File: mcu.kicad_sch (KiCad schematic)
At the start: 0 parts

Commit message: feat: microcontroller setup with decoupling caps
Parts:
- added BZ1: Buzzer, Eagle_Main:Buzzer_TDK_SD1614TT_D16mm_H14mm_P5mm, symbol Device:Buzzer
- added C16, C17, C18, C19, C20, C21, C22, C23, C27, C6, C7, C8, C9: 100n, Capacitor_SMD:C_0603_1608Metric, symbol Device:C
- added C24: 4.7u, Capacitor_SMD:C_0805_2012Metric, symbol Device:C
- added C25, C26: 2.2u, Capacitor_SMD:C_0805_2012Metric, symbol Device:C
- added C28, C29: 1u, Capacitor_SMD:C_0805_2012Metric, symbol Device:C
- added C4, C5: C, Capacitor_SMD:C_0603_1608Metric, symbol Device:C
- added D4: 1N4148W, Diode_SMD:D_SOD-323, symbol Diode:1N4148W
- added D5, D6: LED_Small, LED_SMD:LED_0603_1608Metric, symbol Device:LED_Small
- added D7: TVS, Diode_SMD:D_SOD-523, symbol Device:D_Zener
- added IC2: STM32H723ZGT6, Package_QFP:LQFP-144_20x20mm_P0.5mm, symbol STM32H7:STM32H723ZGT6
- added J1: Conn_ST_STDC14, eagle_connectors:SAMTEC_FTSH-107-01-L-DV-K-TR, symbol Connector:Conn_ST_STDC14
- added JP1: BOOT0, Jumper:SolderJumper-3_P1.3mm_Open_RoundedPad1.0x1.5mm, symbol Jumper:SolderJumper_3_Open
- added Q1: 2N7002NXAKR, Package_TO_SOT_SMD:SOT-23, symbol Transistor_FET:2N7002
- added R10, R11: 1k, Resistor_SMD:R_0603_1608Metric, symbol Device:R
- added R12, R3: R, Resistor_SMD:R_0603_1608Metric, symbol Device:R
- added R4: 22R, Resistor_SMD:R_0603_1608Metric, symbol Device:R
- added R5: 100K, Resistor_SMD:R_0603_1608Metric, symbol Device:R
- added R6, R7: 100k, Resistor_SMD:R_0603_1608Metric, symbol Device:R
- added SW1: RESET, Button_Switch_SMD:SW_SPST_FSMSM, symbol Switch:SW_Push
- added Y1: 16MHz, Crystal:Crystal_SMD_EuroQuartz_MT-4Pin_3.2x2.5mm, symbol Device:Crystal_GND24
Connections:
- new net: BZ1.2 (+), D4.2 (A), Q1.3 (D)
- new net: Q1.1 (G), R4.2, R5.2
- new net: C4.1, R3.2, Y1.1
- new net: D5.2 (A), R10.1
- new net: JP1.2 (C), R12.1
- new net: D6.2 (A), R11.1
- new net +3V3: C16.1, C17.1, C18.1, C19.1, C20.1, C21.1, C22.1, C23.1, C24.1, C27.1, C28.1, C29.1, C7.1, C8.1, C9.1, IC2.108 (VDD_8), IC2.121 (VDD_9), IC2.131 (VDD_10), IC2.144 (VDD_11), IC2.17 (VDD_1), IC2.32 (VREF+), IC2.33 (VDDA), IC2.39 (VDD_3), IC2.52 (VDD_4), IC2.62 (VDD_5), IC2.72 (VDD_6), IC2.84 (VDD_7), J1.3 (VCC), JP1.1 (A), R6.2
- new net +5V: BZ1.1 (-), D4.1 (K)
- new net 3V3_PROBING: R6.1, R7.2
- new net BOOT0: IC2.138 (BOOT0), R12.2
- new net BUZZER: R4.1
- new net GND: C16.2, C17.2, C18.2, C19.2, C20.2, C21.2, C22.2, C23.2, C24.2, C25.2, C26.2, C27.2, C28.2, C29.2, C4.2, C5.2, C6.2, C7.2, C8.2, C9.2, D5.1 (K), D6.1 (K), D7.2 (A), IC2.107 (VSS_7), IC2.120 (VSS_8), IC2.130 (VSS_9), IC2.16 (VSS_1), IC2.31 (VSSA), IC2.38 (VSS_2), IC2.51 (VSS_3), IC2.61 (VSS_4), IC2.83 (VSS_5), J1.11 (GNDDetect), J1.5 (GND), J1.7 (GND), JP1.3 (B), Q1.2 (S), R5.1, R7.1, SW1.1, Y1.2, Y1.4
- new net LED_1: R10.2
- new net LED_2: R11.2
- new net OSC_IN: C5.1, IC2.23 (PH0-OSC_IN), Y1.3
- new net OSC_OUT: IC2.24 (PH1-OSC_OUT), R3.1
- new net RX_SWD: J1.13 (VCP_RX)
- new net SWCLK: J1.6 (JCLK/SWCLK)
- new net SWDIO: J1.4 (JTMS/SWDIO)
- new net TX_SWD: J1.14 (VCP_TX)
- new net VCAP1: C25.1, IC2.71 (VCAP_1)
- new net VCAP2: C26.1, IC2.106 (VCAP_2)
- new net ~{RST}: C6.1, D7.1 (K), IC2.25 (NRST), J1.12 (~{RST}), SW1.2
- no-connect marks 0 -> 3
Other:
- note added: "3V3 probing divider"
- note added: "Analog supply"
- note added: "BOOT0"
- note added: "Bulk cap"
- note added: "Buzzer"
- note added: "Crystal"
- note added: "Debugger"
- note added: "Decoupling"
- note added: "Internal regulator capacitors"
- note added: "LEDs signals"
- note added: "PB8-BOOT0 pin configuration: LOW: normal, boot from user flash HIGH: boot from system memory, bootloader"
- note added: "RESET"
- note added: "Supply decoupling"

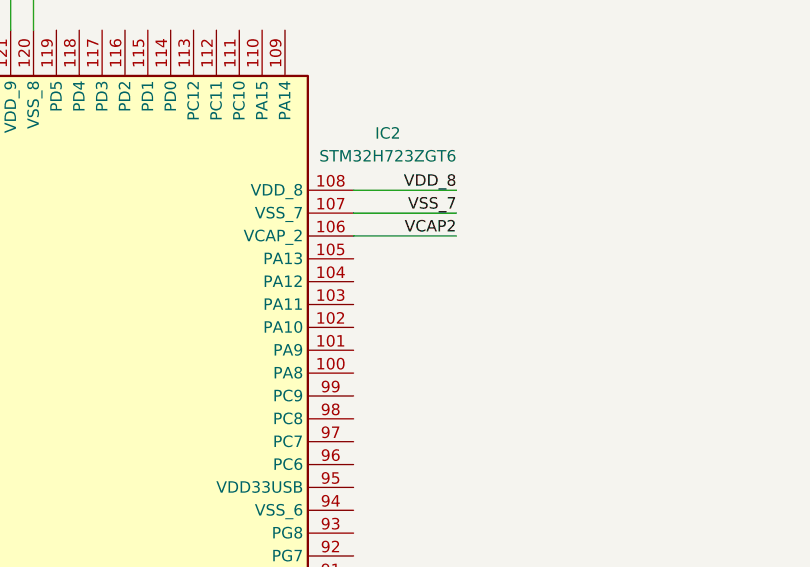
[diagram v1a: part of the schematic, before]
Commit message: feat: voltage divider on UA96 inputs from new llinear encoder
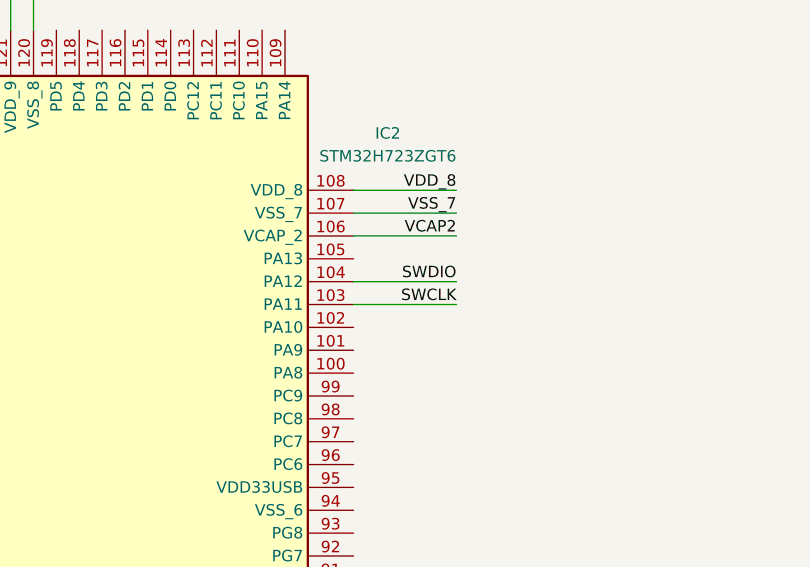
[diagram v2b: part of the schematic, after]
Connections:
- net SWCLK: now also IC2.103 (PA11)
- net SWDIO: now also IC2.104 (PA12)
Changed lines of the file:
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@@
+	(wire
+		(pts
+			(xy 261.62 110.49) (xy 273.05 110.49)
+		)
+		(stroke
+			(width 0)
+			(type default)
+		)
+	)
 	(wire
 		(pts
@@
 		(pts
 			(xy 228.6 204.47) (xy 228.6 214.63)
+		)
+		(stroke
+			(width 0)
+			(type default)
+		)
+	)
+	(wire
+		(pts
+			(xy 261.62 107.95) (xy 273.05 107.95)
 		)
 		(stroke
@@
 		)
 	)
+	(label "SWDIO"
+		(at 273.05 107.95 180)
+		(effects
+			(font
+				(size 1.27 1.27)
+			)
+			(justify right bottom)
+		)
+	)
 	(label "VREF+"
 		(at 146.05 176.53 0)
@@
 		(effects
 			(font
+				(size 1.27 1.27)
+			)
+			(justify right bottom)
+		)
+	)
+	(label "SWCLK"
+		(at 273.05 110.49 180)
+		(effects
+			(font

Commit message: fix: minors
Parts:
- removed BZ1: Buzzer, Eagle_Main:Buzzer_TDK_SD1614TT_D16mm_H14mm_P5mm, symbol Device:Buzzer
- removed D4: 1N4148W, Diode_SMD:D_SOD-323, symbol Diode:1N4148W
- removed Q1: 2N7002NXAKR, Package_TO_SOT_SMD:SOT-23, symbol Transistor_FET:2N7002
- removed R4: 22R, Resistor_SMD:R_0603_1608Metric, symbol Device:R
- removed R5: 100K, Resistor_SMD:R_0603_1608Metric, symbol Device:R
- removed R6, R7: 100k, Resistor_SMD:R_0603_1608Metric, symbol Device:R
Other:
- note removed: "3V3 probing divider"
- note removed: "Buzzer"
- moved on the sheet: D5, D6, R10, R11

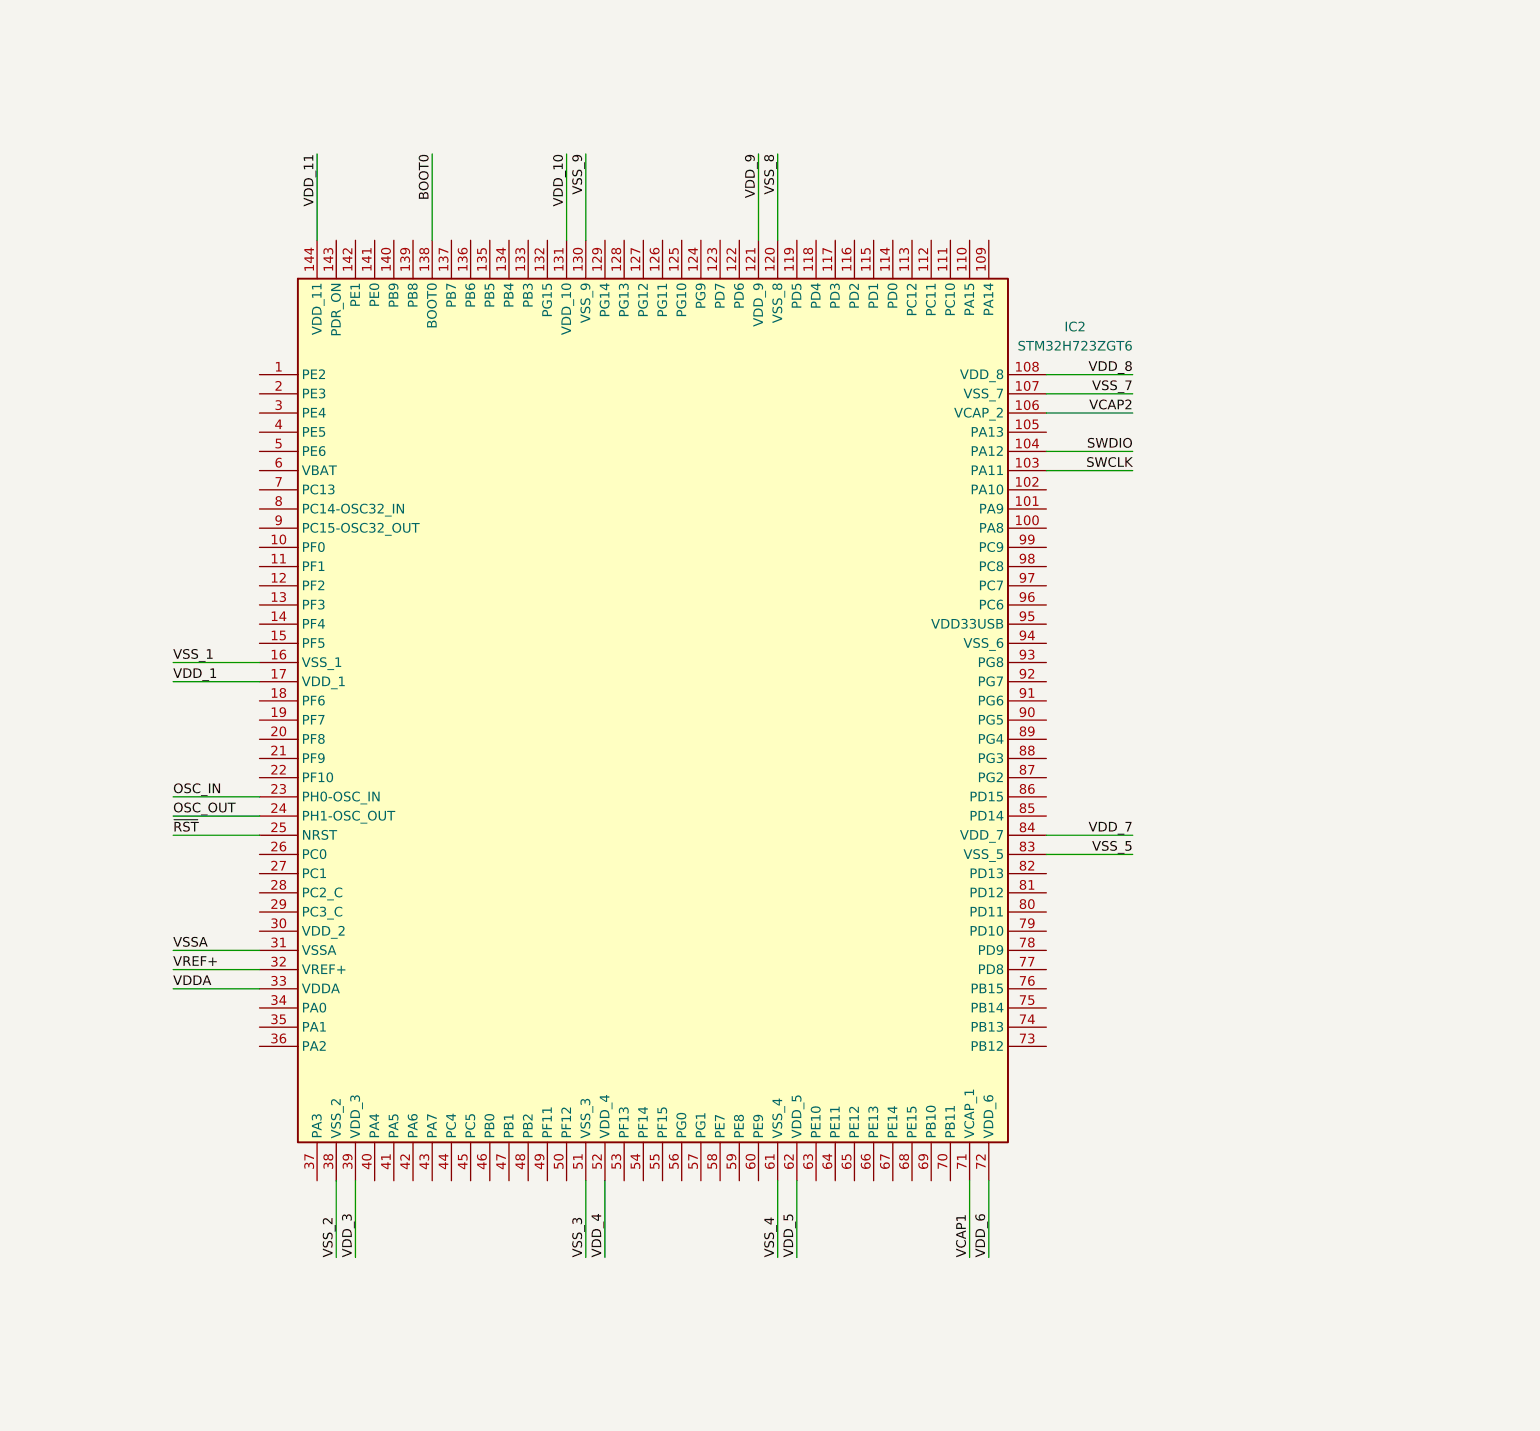
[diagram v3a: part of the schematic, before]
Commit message: feat: pwm for dcs to micro, uart
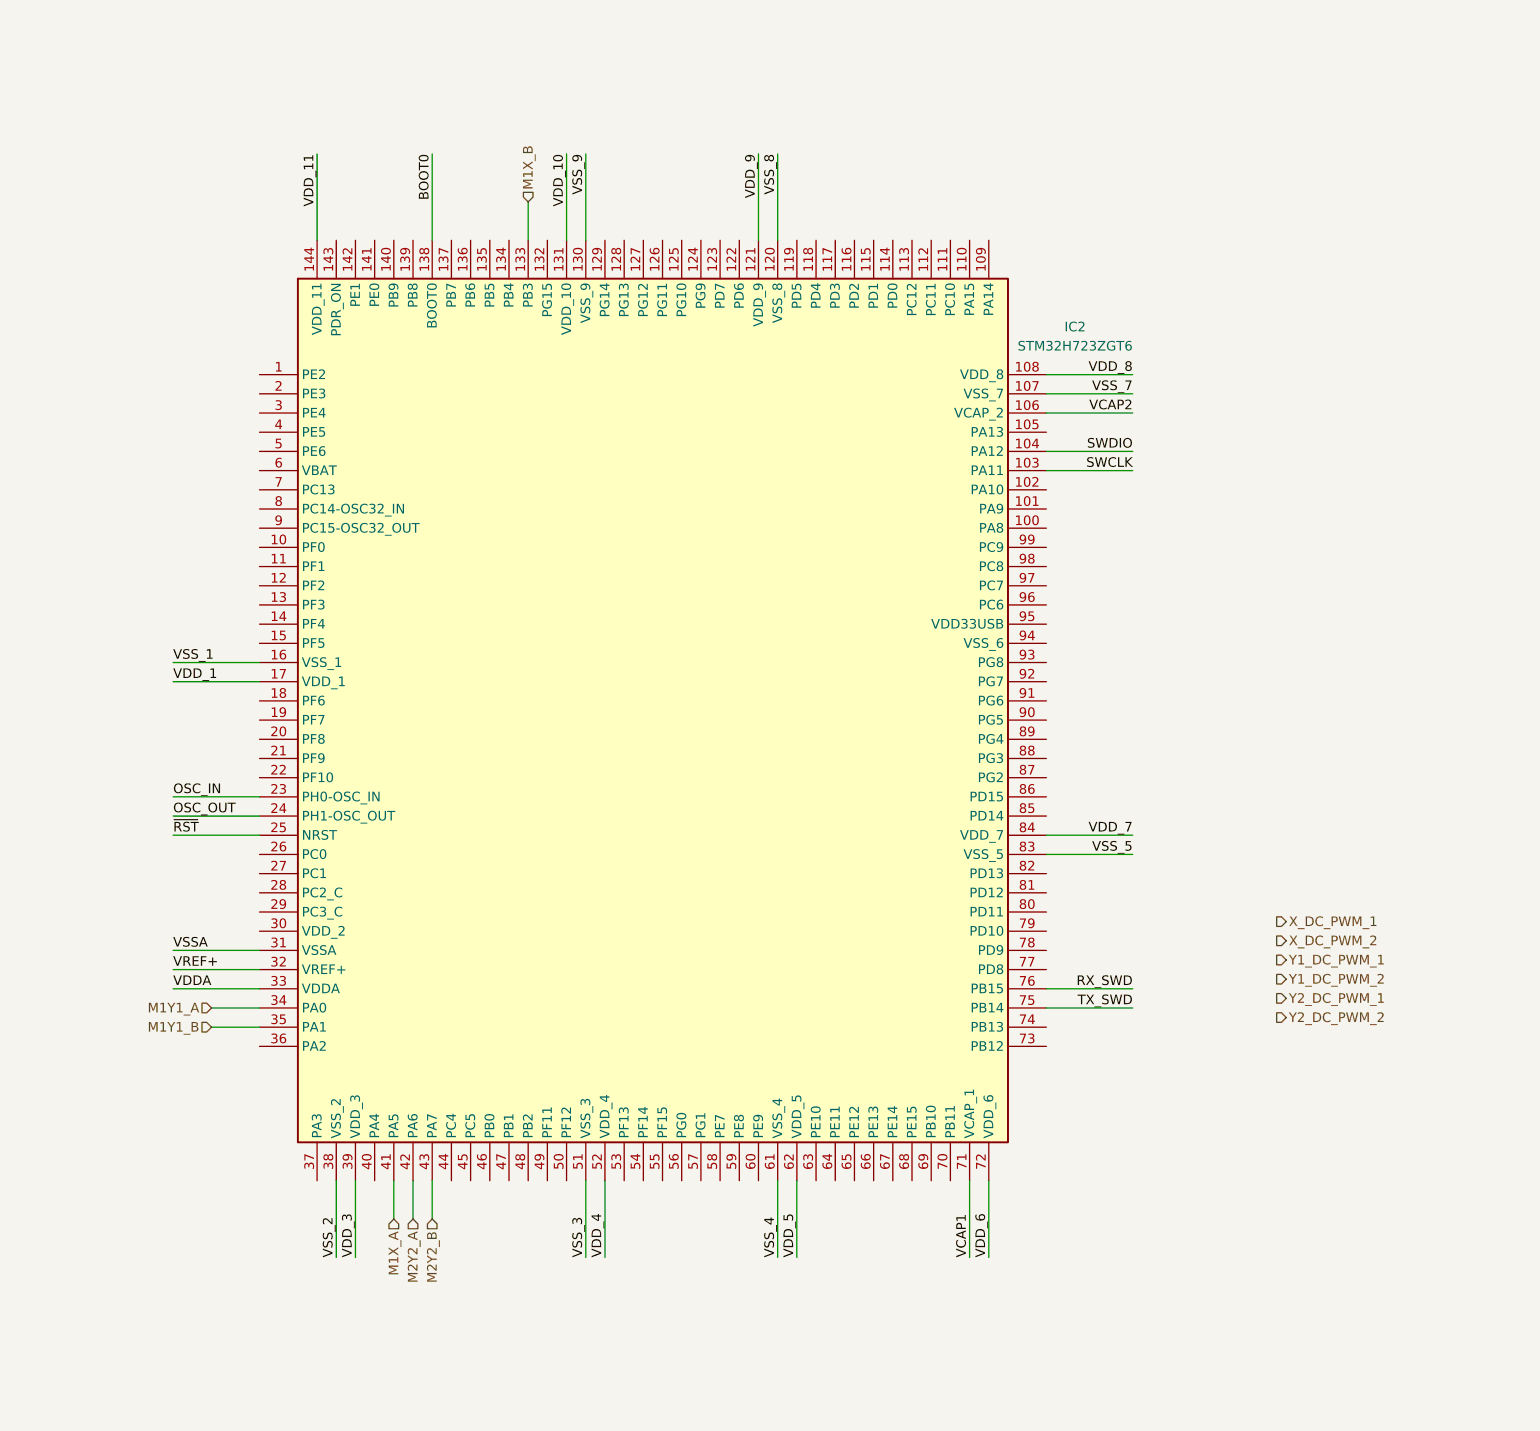
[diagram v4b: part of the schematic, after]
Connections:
- net RX_SWD: now also IC2.76 (PB15)
- net TX_SWD: now also IC2.75 (PB14)
- net M1X_B: now reaches IC2.133 (PB3)
- net M1Y1_A: now reaches IC2.34 (PA0)
- net M1Y1_B: now reaches IC2.35 (PA1)
- net M1X_A: now reaches IC2.41 (PA5)
- net M2Y2_A: now reaches IC2.42 (PA6)
- net M2Y2_B: now reaches IC2.43 (PA7)
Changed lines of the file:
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@@
+	(wire
+		(pts
+			(xy 180.34 204.47) (xy 180.34 209.55)
+		)
+		(stroke
+			(width 0)
+			(type default)
+		)
+	)
 	(wire
 		(pts
@@
 	(wire
 		(pts
+			(xy 151.13 184.15) (xy 157.48 184.15)
+		)
+		(stroke
+			(width 0)
+			(type default)
+		)
+	)
+	(wire
+		(pts
 			(xy 41.91 134.62) (xy 38.1 134.62)
 		)
@@
 	(wire
 		(pts
+			(xy 175.26 204.47) (xy 175.26 209.55)
+		)
+		(stroke
+			(width 0)
+			(type default)
+		)
+	)
+	(wire
+		(pts
 			(xy 27.94 93.98) (xy 27.94 95.25)
 		)
@@
 		)
 	)
+	(wire
+		(pts
+			(xy 261.62 181.61) (xy 273.05 181.61)
+		)
+		(stroke
+			(width 0)
+			(type default)
+		)
+	)
 	(polyline
 		(pts
@@
 	(wire
 		(pts
+			(xy 177.8 204.47) (xy 177.8 209.55)
+		)
+		(stroke
+			(width 0)
+			(type default)
+		)
+	)
+	(wire
+		(pts
 			(xy 38.1 154.94) (xy 41.91 154.94)
 		)
@@
 	(wire
 		(pts
+			(xy 151.13 181.61) (xy 157.48 181.61)
+		)
+		(stroke
+			(width 0)
+			(type default)
+		)
+	)
+	(wire
+		(pts
 			(xy 73.66 50.8) (xy 73.66 49.53)
 		)
@@
 	(wire
 		(pts
+			(xy 261.62 179.07) (xy 273.05 179.07)
+		)
+		(stroke
+			(width 0)
+			(type default)
+		)
+	)
+	(wire
+		(pts
 			(xy 67.31 199.39) (xy 67.31 198.12)
 		)
@@
 		(pts
 			(xy 180.34 68.58) (xy 180.34 80.01)
+		)
+		(stroke
+			(width 0)
+			(type default)
+		)
+	)
+	(wire
+		(pts
+			(xy 193.04 74.93) (xy 193.04 80.01)
 		)
 		(stroke
@@
 		)
 	)
+	(label "TX_SWD"
+		(at 273.05 181.61 180)
+		(effects
+			(font
+				(size 1.27 1.27)
+			)
+			(justify right bottom)
+		)
+	)
 	(label "LED_2"
 		(at 389.89 133.35 0)
@@
 		)
 	)
+	(label "RX_SWD"
+		(at 273.05 179.07 180)
+		(effects
+			(font
+				(size 1.27 1.27)
+			)
+			(justify right bottom)
+		)
+	)
 	(label "VCAP2"
 		(at 273.05 102.87 180)
@@
 		)
 	)
+	(hierarchical_label "X_DC_PWM_1"
+		(shape output)
+		(at 292.1 170.18 0)
+		(effects
+			(font
+				(size 1.27 1.27)
+			)
+			(justify left)
+		)
+	)
+	(hierarchical_label "M2Y2_A"
+		(shape input)
+		(at 177.8 209.55 270)
+		(effects
+			(font
+				(size 1.27 1.27)
+			)
+			(justify right)
+		)
+	)
+	(hierarchical_label "M1X_B"
+		(shape input)
+		(at 193.04 74.93 90)
+		(effects
+			(font
+				(size 1.27 1.27)
+			)
+			(justify left)
+		)
+	)
+	(hierarchical_label "X_DC_PWM_2"
+		(shape output)
+		(at 292.1 172.72 0)
+		(effects
+			(font
+				(size 1.27 1.27)
+			)
+			(justify left)
+		)
+	)
+	(hierarchical_label "M1X_A"
+		(shape input)
+		(at 175.26 209.55 270)
+		(effects
+			(font
+				(size 1.27 1.27)
+			)
+			(justify right)
+		)
+	)
+	(hierarchical_label "Y1_DC_PWM_2"
+		(shape output)
+		(at 292.1 177.8 0)
+		(effects
+			(font
+				(size 1.27 1.27)
+			)
+			(justify left)
+		)
+	)
+	(hierarchical_label "Y2_DC_PWM_1"
+		(shape output)
+		(at 292.1 180.34 0)
+		(effects
+			(font
+				(size 1.27 1.27)
+			)
+			(justify left)
+		)
+	)
+	(hierarchical_label "M1Y1_B"
+		(shape input)
+		(at 151.13 184.15 180)
+		(effects
+			(font
+				(size 1.27 1.27)
+			)
+			(justify right)
+		)
+	)
+	(hierarchical_label "Y2_DC_PWM_2"
+		(shape output)
+		(at 292.1 182.88 0)
+		(effects
+			(font
+				(size 1.27 1.27)
+			)
+			(justify left)
+		)
+	)
+	(hierarchical_label "M1Y1_A"
+		(shape input)
+		(at 151.13 181.61 180)
+		(effects
+			(font
+				(size 1.27 1.27)
+			)
+			(justify right)
+		)
+	)
+	(hierarchical_label "Y1_DC_PWM_1"
+		(shape output)
+		(at 292.1 175.26 0)
+		(effects
+			(font
+				(size 1.27 1.27)
+			)
+			(justify left)
+		)
+	)
+	(hierarchical_label "M2Y2_B"
+		(shape input)
+		(at 180.34 209.55 270)
+		(effects
+			(font
+				(size 1.27 1.27)
+			)
+			(justify right)
+		)
+	)

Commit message: feat: setup spi
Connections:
- net SWCLK: now also IC2.109 (PA14); no longer IC2.103 (PA11)
- net SWDIO: now also IC2.105 (PA13); no longer IC2.104 (PA12)
- net SPI1_MOSI: now reaches IC2.123 (PD7)
- net SPI1_MISO: now reaches IC2.124 (PG9)
- net SPI1_SCK: now reaches IC2.126 (PG11)
- net SPI2_MOSI: now reaches IC2.27 (PC1)
- net SPI2_MISO: now reaches IC2.28 (PC2_C)
- net SPI2_SCK: now reaches IC2.69 (PB10)
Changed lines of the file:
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@@
+	(wire
+		(pts
+			(xy 153.67 163.83) (xy 157.48 163.83)
+		)
+		(stroke
+			(width 0)
+			(type default)
+		)
+	)
 	(wire
 		(pts
@@
 	(wire
 		(pts
+			(xy 246.38 204.47) (xy 246.38 208.28)
+		)
+		(stroke
+			(width 0)
+			(type default)
+		)
+	)
+	(wire
+		(pts
 			(xy 87.63 39.37) (xy 77.47 39.37)
 		)
@@
 	(wire
 		(pts
-			(xy 261.62 110.49) (xy 273.05 110.49)
+			(xy 254 80.01) (xy 254 68.58)
 		)
 		(stroke
@@
 	(wire
 		(pts
-			(xy 261.62 107.95) (xy 273.05 107.95)
+			(xy 261.62 105.41) (xy 273.05 105.41)
 		)
 		(stroke
@@
 	(wire
 		(pts
+			(xy 215.9 76.2) (xy 215.9 80.01)
+		)
+		(stroke
+			(width 0)
+			(type default)
+		)
+	)
+	(wire
+		(pts
 			(xy 73.66 67.31) (xy 77.47 67.31)
 		)
@@
 		)
 	)
+	(wire
+		(pts
+			(xy 210.82 76.2) (xy 210.82 80.01)
+		)
+		(stroke
+			(width 0)
+			(type default)
+		)
+	)
 	(polyline
 		(pts
@@
 	(wire
 		(pts
+			(xy 218.44 76.2) (xy 218.44 80.01)
+		)
+		(stroke
+			(width 0)
+			(type default)
+		)
+	)
+	(wire
+		(pts
 			(xy 97.79 49.53) (xy 101.6 49.53)
 		)
@@
 		(pts
 			(xy 73.66 78.74) (xy 73.66 77.47)
+		)
+		(stroke
+			(width 0)
+			(type default)
+		)
+	)
+	(wire
+		(pts
+			(xy 153.67 166.37) (xy 157.48 166.37)
 		)
 		(stroke
@@
 	)
 	(label "SWDIO"
-		(at 273.05 107.95 180)
+		(at 273.05 105.41 180)
 		(effects
 			(font
@@
 	)
 	(label "SWCLK"
-		(at 273.05 110.49 180)
+		(at 254 68.58 270)
 		(effects
 			(font
@@
 		)
 	)
+	(hierarchical_label "SPI2_MOSI"
+		(shape output)
+		(at 153.67 163.83 180)
+		(effects
+			(font
+				(size 1.27 1.27)
+			)
+			(justify right)
+		)
+	)
 	(hierarchical_label "M2Y2_A"
 		(shape input)
@@
 		)
 	)
+	(hierarchical_label "SPI1_MOSI"
+		(shape output)
+		(at 218.44 76.2 90)
+		(effects
+			(font
+				(size 1.27 1.27)
+			)
+			(justify left)
+		)
+	)
 	(hierarchical_label "Y2_DC_PWM_1"
 		(shape output)
@@
 		)
 	)
+	(hierarchical_label "SPI2_SCK"
+		(shape output)
+		(at 246.38 208.28 270)
+		(effects
+			(font
+				(size 1.27 1.27)
+			)
+			(justify right)
+		)
+	)
 	(hierarchical_label "M1Y1_B"
 		(shape input)
@@
 		)
 	)
+	(hierarchical_label "SPI1_SCK"
+		(shape output)
+		(at 210.82 76.2 90)
+		(effects
+			(font
+				(size 1.27 1.27)
+			)
+			(justify left)
+		)
+	)
 	(hierarchical_label "Y2_DC_PWM_2"
 		(shape output)
@@
 		)
 	)
+	(hierarchical_label "SPI2_MISO"
+		(shape input)
+		(at 153.67 166.37 180)
+		(effects
+			(font
+				(size 1.27 1.27)
+			)
+			(justify right)
+		)
+	)
+	(hierarchical_label "SPI1_MISO"
+		(shape input)
+		(at 215.9 76.2 90)
+		(effects
+			(font
+				(size 1.27 1.27)
+			)
+			(justify left)
+		)
+	)
